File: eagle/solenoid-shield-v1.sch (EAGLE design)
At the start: 13 parts, among them Q1 ARDUINOR3-NOIOREF-NOTEXT, SW1 SPST_TACT-EVQQ2, SW2 SPST_TACT-EVQQ2

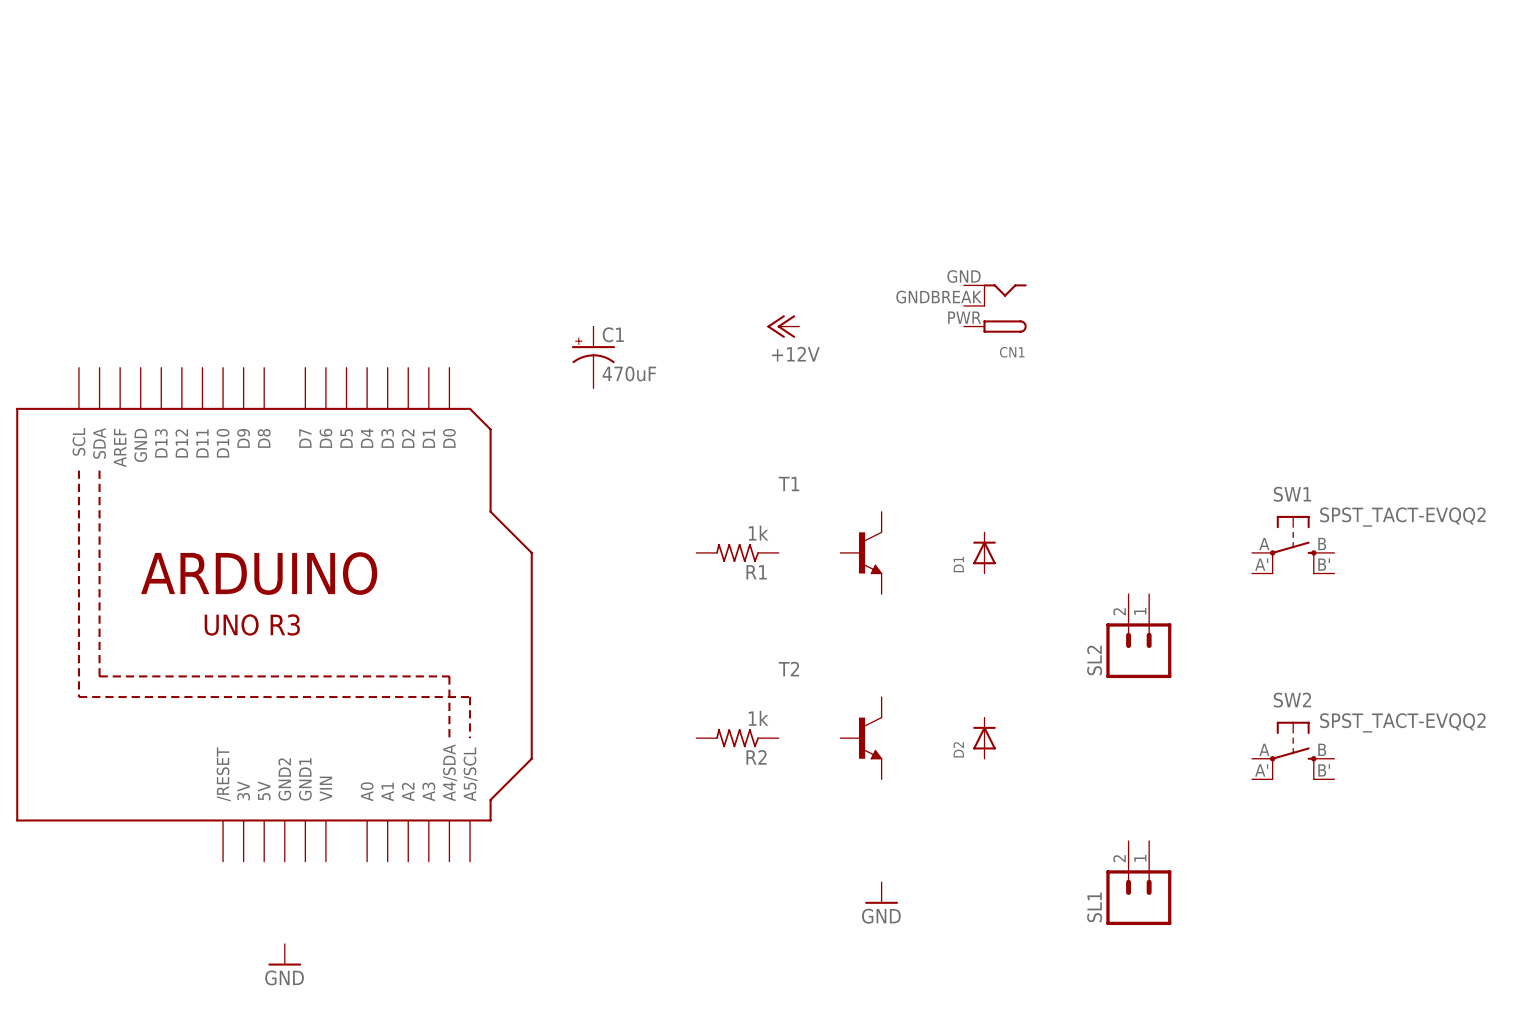
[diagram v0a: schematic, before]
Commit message: Added board, and started routing.
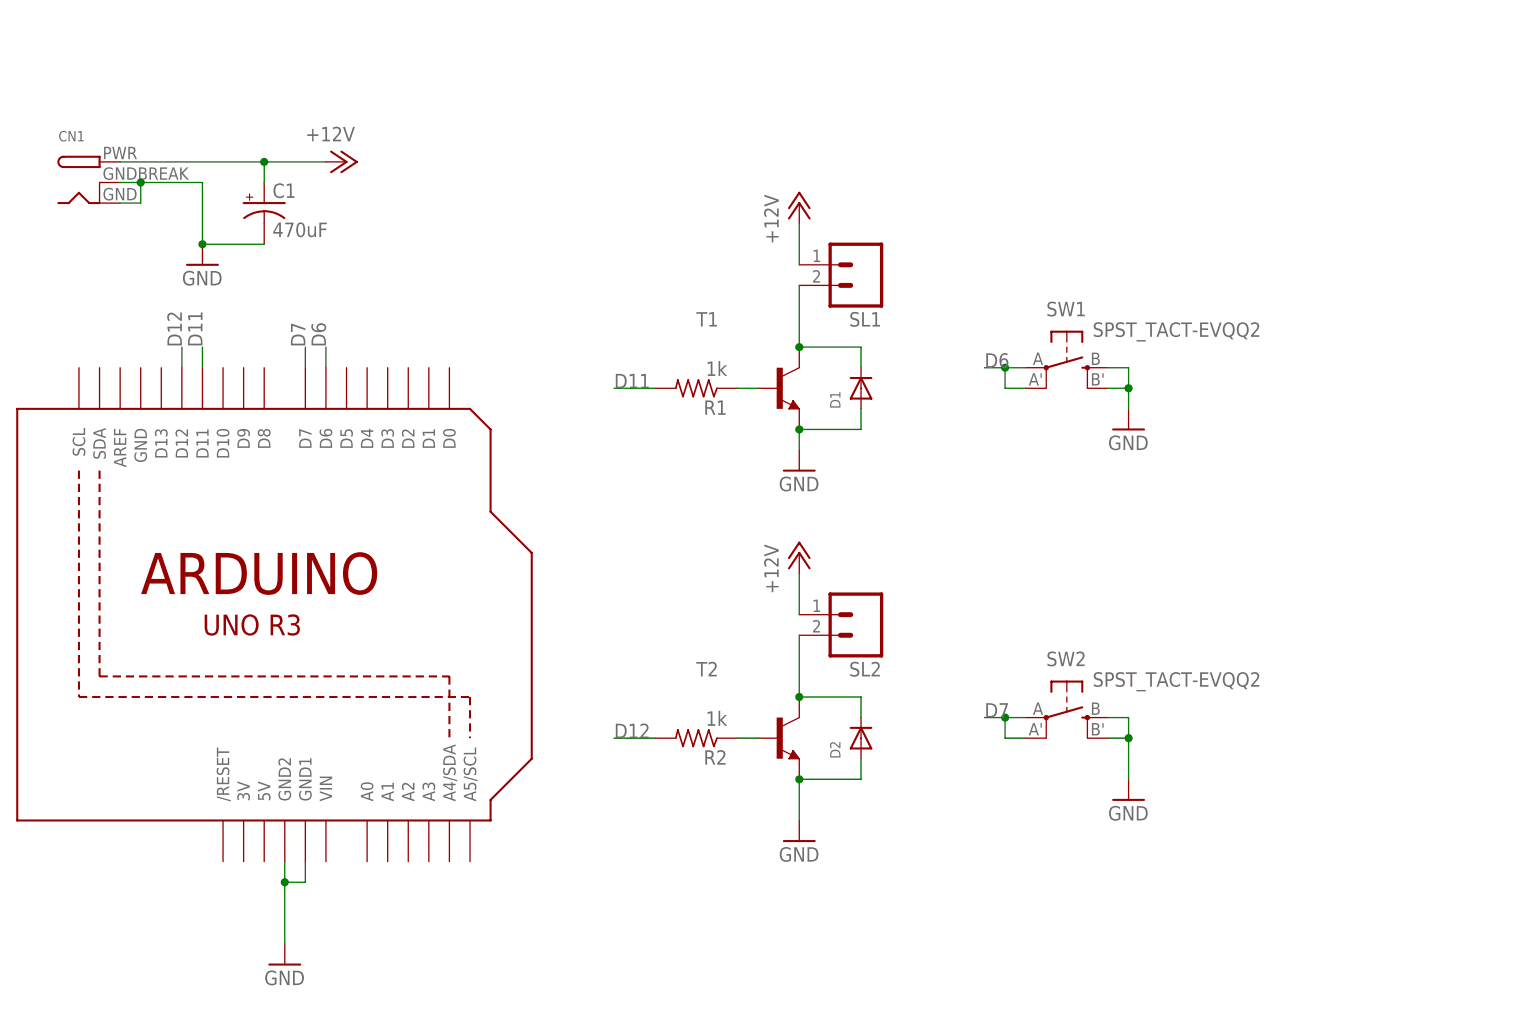
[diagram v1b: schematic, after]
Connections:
- new net +12V: C1.+, CN1.PWR, SL1.1, SL2.1
- new net D11: Q1.D11, R1.2
- new net D12: Q1.D12, R2.2
- new net D6: Q1.D6, SW1.P, SW1.P1
- new net D7: Q1.D7, SW2.P, SW2.P1
- new net GND: C1.-, CN1.GND, CN1.GNDBREAK, D1.A, D2.A, Q1.GND1, Q1.GND2, SW1.S, SW1.S1, SW2.S, SW2.S1, T1.E, T2.E
- new net N$2: R1.1, T1.B
- new net N$3: D1.C, SL1.2, T1.C
- new net N$7: D2.C, SL2.2, T2.C
- new net N$8: R2.1, T2.B
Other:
- moved on the sheet: C1, CN1, D1, D2, R1, R2, SL1, SL2, SW1, SW2, T1, T2

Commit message: Finished v1 of the shield
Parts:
- added LED1, LED2: (no value), adafruit:LEDSMT1206
- added R3: 3k3, adafruit:R-US_R0603
- added R4: 1k, adafruit:R-US_R0603
- added SL3: (no value), con-amp-quick:M02
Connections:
- new net N$1: LED2.A, R4.2
- new net N$4: LED1.A, R3.2
- net +12V: now also SL3.1
- net D11: now also R3.1
- net D12: now also R4.1
- net GND: now also LED2.C, SL3.2
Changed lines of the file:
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@@
 <part name="P+3" library="supply1" deviceset="+12V" device=""/>
 <part name="GND6" library="supply1" deviceset="GND" device=""/>
+<part name="LED1" library="adafruit" deviceset="LED" device="SMT1206"/>
+<part name="LED2" library="adafruit" deviceset="LED" device="SMT1206"/>
+<part name="R3" library="adafruit" deviceset="R-US_" device="R0603" value="3k3"/>
+<part name="R4" library="adafruit" deviceset="R-US_" device="R0603" value="1k"/>
+<part name="SL3" library="con-amp-quick" deviceset="M02" device=""/>
 </parts>
 <sheets>
@@
 <instance part="P+3" gate="1" x="109.22" y="63.5"/>
 <instance part="GND6" gate="1" x="149.86" y="33.02"/>
+<instance part="LED1" gate="G$1" x="101.6" y="76.2" rot="R90"/>
+<instance part="LED2" gate="G$1" x="101.6" y="33.02" rot="R90"/>
+<instance part="R3" gate="G$1" x="91.44" y="76.2"/>
+<instance part="R4" gate="G$1" x="91.44" y="33.02"/>
+<instance part="SL3" gate="G$1" x="33.02" y="127" rot="R270"/>
 </instances>
 <busses>
@@
 <wire x1="43.18" y1="101.6" x2="35.56" y2="101.6" width="0.1524" layer="91"/>
 <junction x="35.56" y="101.6"/>
+<pinref part="SL3" gate="G$1" pin="2"/>
+<wire x1="35.56" y1="119.38" x2="35.56" y2="109.22" width="0.1524" layer="91"/>
+<junction x="35.56" y="109.22"/>
 </segment>
 <segment>
@@
 <pinref part="GND1" gate="1" pin="GND"/>
 <pinref part="T2" gate="G$1" pin="E"/>
-<wire x1="109.22" y1="30.48" x2="109.22" y2="35.56" width="0.1524" layer="91"/>
+<wire x1="109.22" y1="30.48" x2="109.22" y2="33.02" width="0.1524" layer="91"/>
 <pinref part="D2" gate="G$1" pin="A"/>
+<wire x1="109.22" y1="33.02" x2="109.22" y2="35.56" width="0.1524" layer="91"/>
 <wire x1="109.22" y1="35.56" x2="116.84" y2="35.56" width="0.1524" layer="91"/>
 <wire x1="116.84" y1="35.56" x2="116.84" y2="38.1" width="0.1524" layer="91"/>
 <junction x="109.22" y="35.56"/>
+<pinref part="LED2" gate="G$1" pin="C"/>
+<wire x1="106.68" y1="33.02" x2="109.22" y2="33.02" width="0.1524" layer="91"/>
+<junction x="109.22" y="33.02"/>
 </segment>
 <segment>
@@
 <wire x1="50.8" y1="111.76" x2="43.18" y2="111.76" width="0.1524" layer="91"/>
 <pinref part="C1" gate="G$1" pin="+"/>
-<wire x1="43.18" y1="111.76" x2="25.4" y2="111.76" width="0.1524" layer="91"/>
+<wire x1="43.18" y1="111.76" x2="33.02" y2="111.76" width="0.1524" layer="91"/>
+<wire x1="33.02" y1="111.76" x2="25.4" y2="111.76" width="0.1524" layer="91"/>
 <wire x1="43.18" y1="109.22" x2="43.18" y2="111.76" width="0.1524" layer="91"/>
 <junction x="43.18" y="111.76"/>
+<pinref part="SL3" gate="G$1" pin="1"/>
+<wire x1="33.02" y1="119.38" x2="33.02" y2="111.76" width="0.1524" layer="91"/>
+<junction x="33.02" y="111.76"/>
 </segment>
 <segment>
@@
 <pinref part="R2" gate="G$1" pin="2"/>
 <wire x1="91.44" y1="40.64" x2="86.36" y2="40.64" width="0.1524" layer="91"/>
-<label x="86.36" y="40.64" size="1.778" layer="95"/>
+<label x="83.82" y="40.64" size="1.778" layer="95"/>
+<pinref part="R4" gate="G$1" pin="1"/>
+<wire x1="86.36" y1="33.02" x2="86.36" y2="40.64" width="0.1524" layer="91"/>
+<wire x1="86.36" y1="40.64" x2="83.82" y2="40.64" width="0.1524" layer="91"/>
+<junction x="86.36" y="40.64"/>
 </segment>
 </net>
@@
 <pinref part="R1" gate="G$1" pin="2"/>
 <wire x1="91.44" y1="83.82" x2="86.36" y2="83.82" width="0.1524" layer="91"/>
-<label x="86.36" y="83.82" size="1.778" layer="95"/>
+<label x="83.82" y="83.82" size="1.778" layer="95"/>
+<pinref part="R3" gate="G$1" pin="1"/>
+<wire x1="86.36" y1="76.2" x2="86.36" y2="83.82" width="0.1524" layer="91"/>
+<wire x1="86.36" y1="83.82" x2="83.82" y2="83.82" width="0.1524" layer="91"/>
+<junction x="86.36" y="83.82"/>
 </segment>
 </net>
@@
 </segment>
 </net>
+<net name="N$1" class="0">
+<segment>
+<pinref part="LED2" gate="G$1" pin="A"/>
+<pinref part="R4" gate="G$1" pin="2"/>
+<wire x1="99.06" y1="33.02" x2="96.52" y2="33.02" width="0.1524" layer="91"/>
+</segment>
+</net>
+<net name="N$4" class="0">
+<segment>
+<pinref part="LED1" gate="G$1" pin="A"/>
+<pinref part="R3" gate="G$1" pin="2"/>
+<wire x1="99.06" y1="76.2" x2="96.52" y2="76.2" width="0.1524" layer="91"/>
+</segment>
+</net>
